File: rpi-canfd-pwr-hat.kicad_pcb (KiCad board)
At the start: 4 copper layers, 65 x 56 mm, 89 parts, among them J1 Conn_01x02, J2 Conn_01x04_Pin, J3 Raspberry_Pi, J4 Conn_01x02, J5 Conn_01x02, U1 XC6206P332MR, U10 SN74LV1T125DBV, U11 SN74LV1T125DBV, U12 SN74LV1T125DBV, U13 SN74LV1T125DBV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

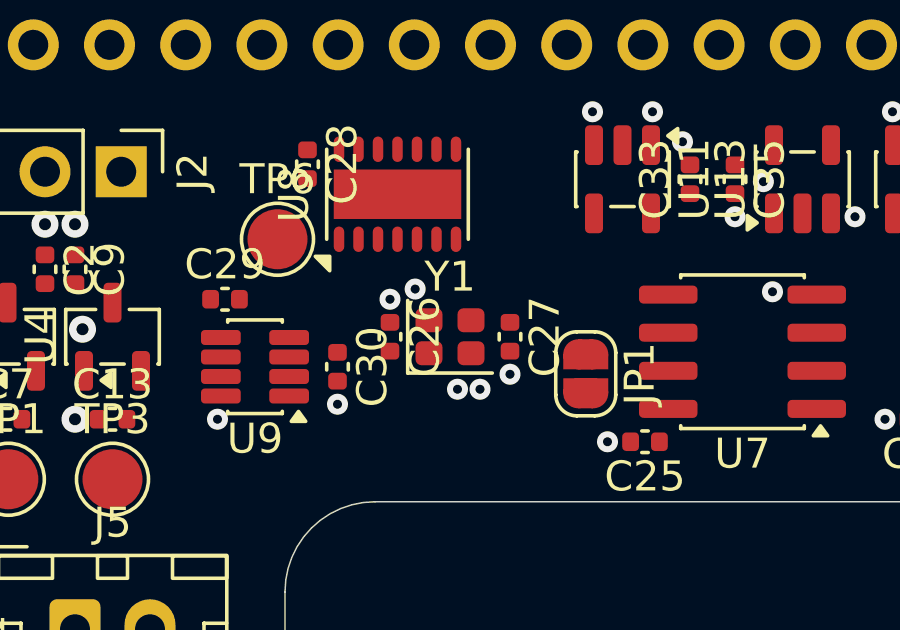
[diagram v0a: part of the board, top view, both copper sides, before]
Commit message: pcb: add xtal routing
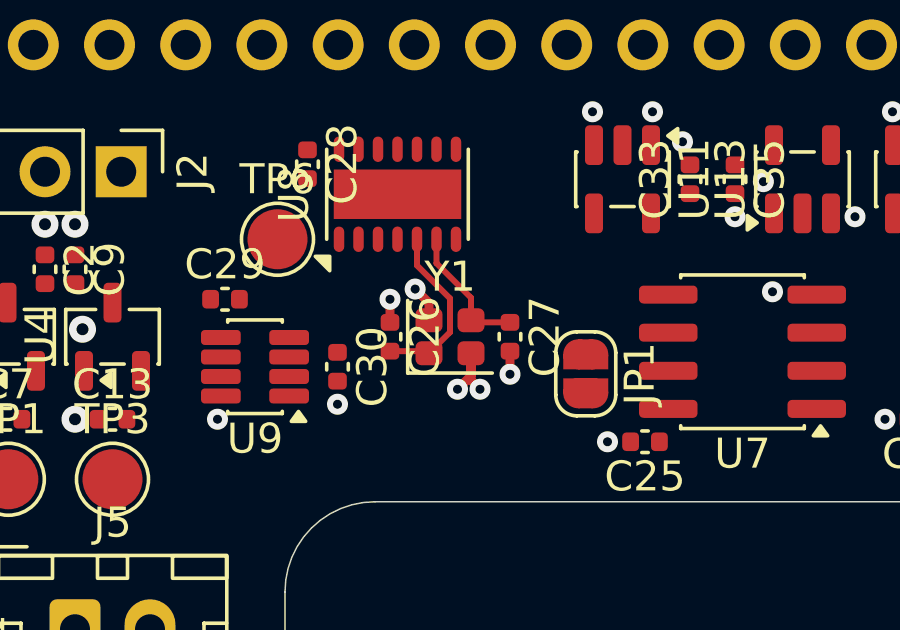
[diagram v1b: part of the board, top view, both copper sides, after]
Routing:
- net /XTAL_P: track 0.00 -> 5.87 mm
- net GND: track 0.00 -> 5.48 mm
- net /XTAL_N: track 0.00 -> 4.51 mm
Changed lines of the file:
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@@
 		(layer "Edge.Cuts")
+	)
+	(segment
+		(start 189.5 85.75)
+		(end 189.5 84.98)
+		(width 0.3)
+		(layer "F.Cu")
+		(net "GND")
+	)
+	(segment
+		(start 188.2 85.8)
+		(end 187.75 86.25)
+		(width 0.3)
+		(layer "F.Cu")
+		(net "GND")
+	)
+	(segment
+		(start 186.8 83.95)
+		(end 186.8 83.371099)
+		(width 0.3)
+		(layer "F.Cu")
+		(net "GND")
+	)
+	(segment
+		(start 185.5 84.02)
+		(end 185.5 83.25)
+		(width 0.3)
+		(layer "F.Cu")
+		(net "GND")
+	)
+	(segment
+		(start 188.2 85.05)
+		(end 188.2 85.95)
+		(width 0.3)
+		(layer "F.Cu")
+		(net "GND")
+	)
+	(segment
+		(start 188.2 85.95)
+		(end 188.5 86.25)
+		(width 0.3)
+		(layer "F.Cu")
+		(net "GND")
+	)
+	(segment
+		(start 186.8 83.371099)
+		(end 186.338833 82.909932)
+		(width 0.3)
+		(layer "F.Cu")
+		(net "GND")
+	)
+	(segment
+		(start 188.2 85.05)
+		(end 188.2 85.8)
+		(width 0.3)
+		(layer "F.Cu")
+		(net "GND")
 	)
 	(via
@@
 		(free yes)
 		(net "GND")
+	)
+	(segment
+		(start 187.5 84.35)
+		(end 186.8 85.05)
+		(width 0.2)
+		(layer "F.Cu")
+		(net "/XTAL_P")
+	)
+	(segment
+		(start 185.5 84.98)
+		(end 186.73 84.98)
+		(width 0.2)
+		(layer "F.Cu")
+		(net "/XTAL_P")
+	)
+	(segment
+		(start 186.4 82.12257)
+		(end 187.5 83.22257)
+		(width 0.2)
+		(layer "F.Cu")
+		(net "/XTAL_P")
+	)
+	(segment
+		(start 186.4 81.25)
+		(end 186.4 82.12257)
+		(width 0.2)
+		(layer "F.Cu")
+		(net "/XTAL_P")
+	)
+	(segment
+		(start 187.5 83.22257)
+		(end 187.5 84.35)
+		(width 0.2)
+		(layer "F.Cu")
+		(net "/XTAL_P")
+	)
+	(segment
+		(start 186.73 84.98)
+		(end 186.8 85.05)
+		(width 0.2)
+		(layer "F.Cu")
+		(net "/XTAL_P")
+	)
+	(segment
+		(start 188.2 83.2)
+		(end 187.05 82.05)
+		(width 0.2)
+		(layer "F.Cu")
+		(net "/XTAL_N")
+	)
+	(segment
+		(start 188.27 84.02)
+		(end 188.2 83.95)
+		(width 0.2)
+		(layer "F.Cu")
+		(net "/XTAL_N")
+	)
+	(segment
+		(start 189.5 84.02)
+		(end 188.27 84.02)
+		(width 0.2)
+		(layer "F.Cu")
+		(net "/XTAL_N")
+	)
+	(segment
+		(start 187.05 82.05)
+		(end 187.05 81.25)
+		(width 0.2)
+		(layer "F.Cu")
+		(net "/XTAL_N")
+	)
+	(segment
+		(start 188.2 83.95)
+		(end 188.2 83.2)
+		(width 0.2)
+		(layer "F.Cu")
+		(net "/XTAL_N")
 	)
 	(zone
@@
 			)
 		)
+	)
+	(zone
+		(layer "F.Cu")
+		(hatch edge 0.5)
+		(connect_pads
+			(clearance 0)
+		)
+		(min_thickness 0.25)
+		(keepout
+			(tracks allowed)
+			(vias allowed)
+			(pads allowed)
+			(copperpour not_allowed)
+			(footprints allowed)
+		)
+		(placement
+			(enabled no)
+			(sheetname "/")
+		)
+		(fill
+			(thermal_gap 0.5)
+			(thermal_bridge_width 0.5)
+			(island_removal_mode 0)
+		)
+		(polygon
+			(pts
+				(xy 189.25 82.5) (xy 190 83.25) (xy 190 86.25) (xy 189.5 86.75) (xy 186 86.75) (xy 185 85.75) (xy 185 83.25)
+				(xy 185.75 82.5)
+			)
+		)

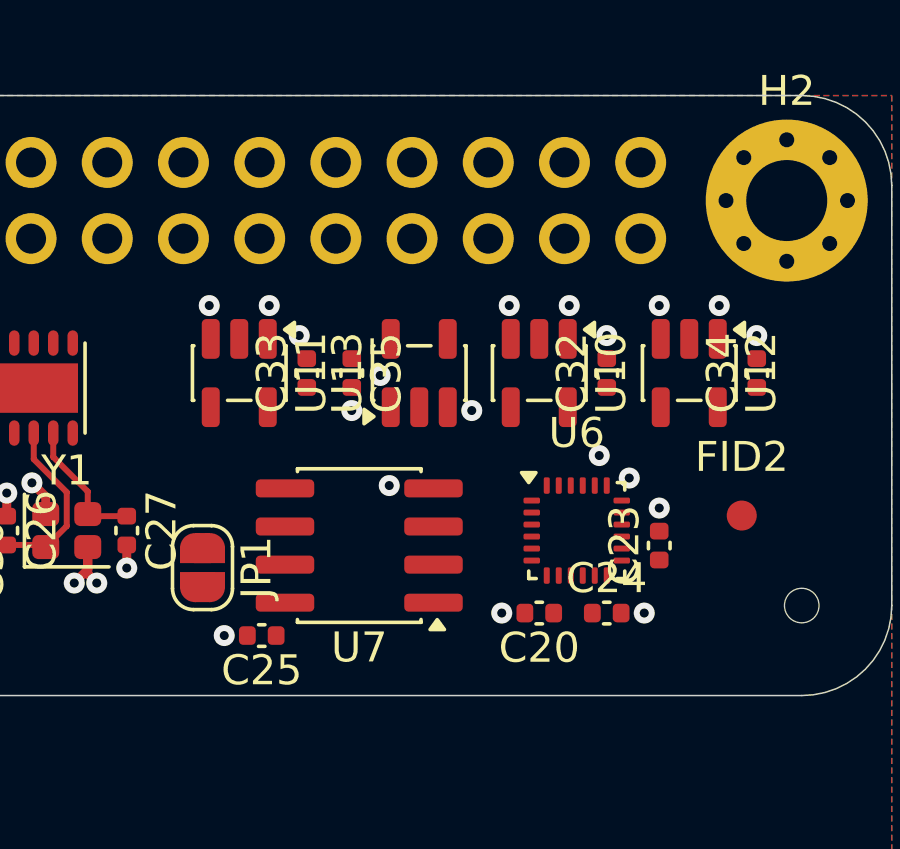
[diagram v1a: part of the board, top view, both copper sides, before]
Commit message: pcb: route imu
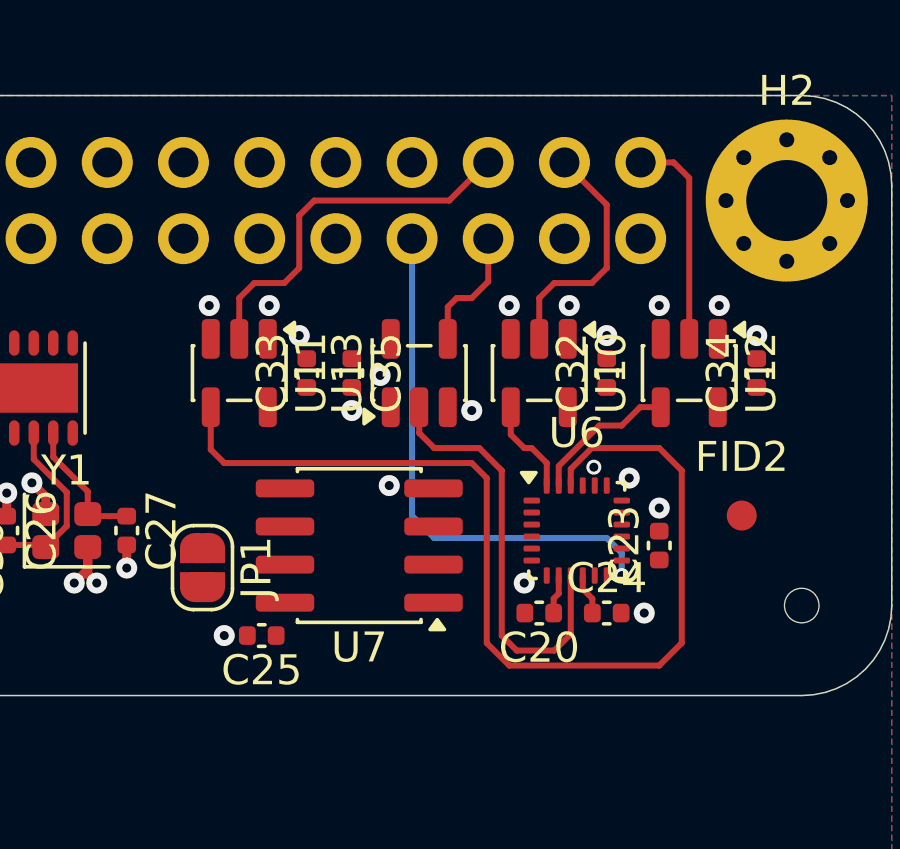
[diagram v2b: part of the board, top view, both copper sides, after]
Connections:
- J3 pad 12: /~{SPI2_CS} -> unconnected-(J3-GPIO18/SPI1_~{CE0}/PCM_CLK/PWM0-Pad12)
- J3 pad 22: /IMU_INT -> unconnected-(J3-GPIO25/SDIO_DAT1-Pad22)
- J3 pad 33: unconnected-(J3-GPIO13/PWM1-Pad33) -> /IMU_INT
- J3 pad 36: unconnected-(J3-GPIO16/SPI1_~{CE2}-Pad36) -> /~{SPI2_CS}
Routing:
- net /~{SPI2_CS}_1V8: track 0.00 -> 34.2 mm
- net /IMU_INT: track 0.00 -> 18.0 mm, vias 0 -> 1
- net /SPI2_MISO_1V8: track 0.00 -> 14.3 mm
- net /~{SPI2_CS}: track 0.00 -> 12.6 mm
- net /SPI2_MOSI: track 0.00 -> 8.13 mm
- net /SPI2_SCLK: track 0.00 -> 7.20 mm
- net /SPI2_SCLK_1V8: track 0.00 -> 4.86 mm
- net /SPI2_MISO: track 0.00 -> 4.19 mm
- net /SPI2_MOSI_1V8: track 0.00 -> 3.26 mm
- net Net-(U6-REGOUT): track 0.00 -> 1.38 mm
- net +1V8: track 0.00 -> 1.32 mm

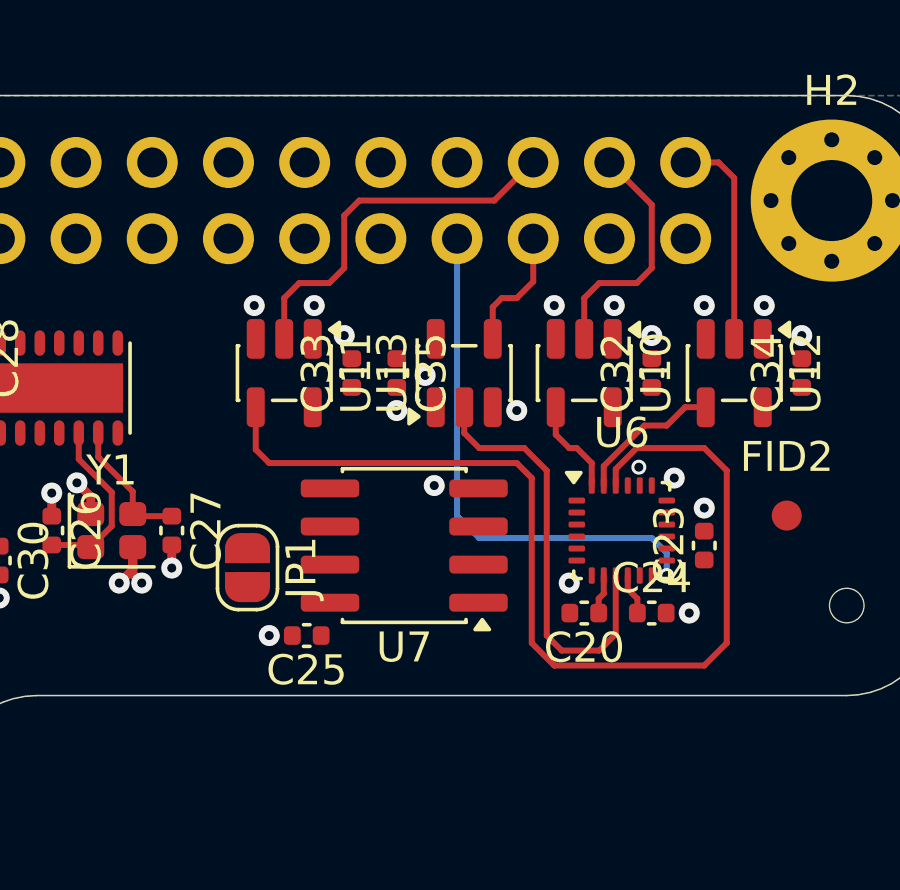
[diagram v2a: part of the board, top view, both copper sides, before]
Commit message: pcb: route eeprom
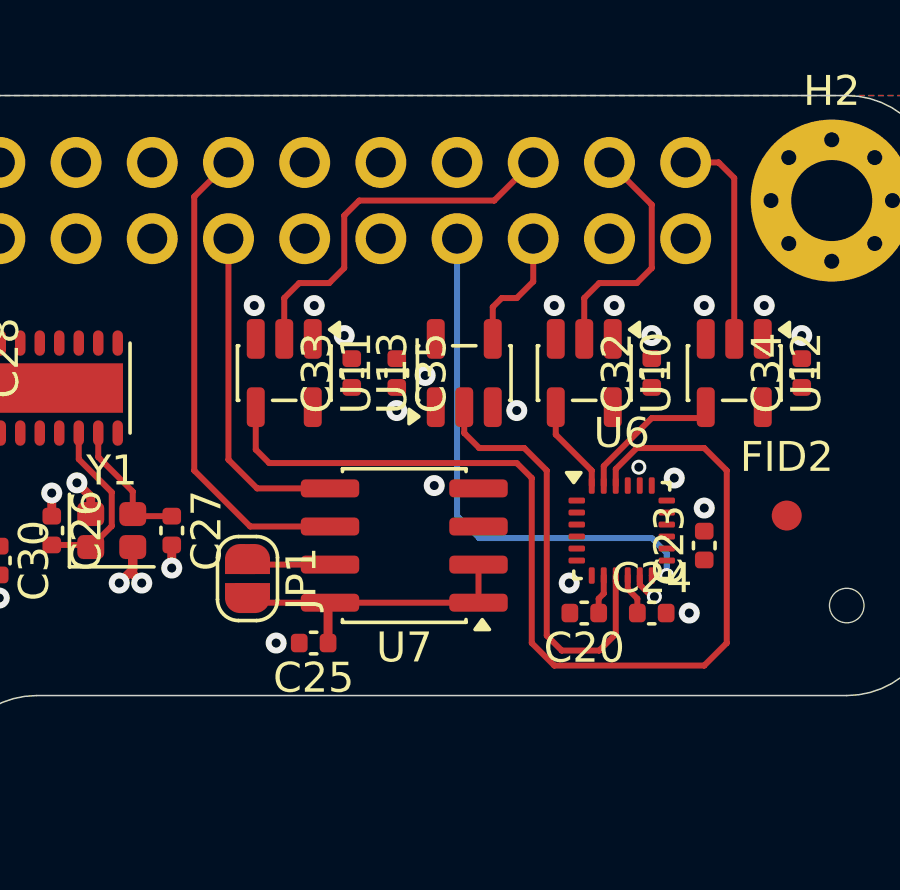
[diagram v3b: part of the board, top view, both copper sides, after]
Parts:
- moved JP1 0.36 mm to (192.0, 86.1)
- moved C25 0.34 mm to (194.2, 88.2)
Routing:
- net /SCL: track 0.00 -> 16.0 mm
- net /SDA: track 0.00 -> 11.2 mm
- net +3V3: track 0.00 -> 10.4 mm
- net Net-(JP1-A): track 0.00 -> 2.83 mm
- net GND: track 5.48 -> 6.44 mm, vias 75 -> 76
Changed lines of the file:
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@@
 	(footprint "Jumper:SolderJumper-2_P1.3mm_Open_RoundedPad1.0x1.5mm"
 		(layer "F.Cu")
-		(at 192.025 85.735 -90)
+		(at 192.025 86.1 -90)
 		(descr "SMD Solder Jumper, 1x1.5mm, rounded Pads, 0.3mm gap, open")
 		(tags "solder jumper open")
@@
 	(footprint "Capacitor_SMD:C_0402_1005Metric"
 		(layer "F.Cu")
-		(at 194 88 180)
+		(at 194.23 88.25 180)
 		(descr "Capacitor SMD 0402 (1005 Metric), square (rectangular) end terminal, IPC-7351 nominal, (Body size source: IPC-SM-782 page 76, https://www.pcb-3d.com/wordpress/wp-content/uploads/ipc-sm-782a_amendment_1_and_2.pdf)")
 		(tags "capacitor")
@@
 	)
 	(segment
+		(start 205.502917 86.703567)
+		(end 205.58807 86.703567)
+		(width 0.2)
+		(layer "F.Cu")
+		(net "GND")
+	)
+	(segment
 		(start 186.8 83.371099)
 		(end 186.338833 82.909932)
@@
 	)
 	(segment
+		(start 205.1 86)
+		(end 205.1 86.30065)
+		(width 0.2)
+		(layer "F.Cu")
+		(net "GND")
+	)
+	(segment
 		(start 188.2 85.05)
 		(end 188.2 85.8)
@@
 		(net "GND")
 	)
+	(segment
+		(start 205.1 86.30065)
+		(end 205.502917 86.703567)
+		(width 0.2)
+		(layer "F.Cu")
+		(net "GND")
+	)
 	(via
 		(at 171.75 84.25)
@@
 	)
 	(via
+		(at 205.58807 86.703567)
+		(size 0.5)
+		(drill 0.3)
+		(layers "F.Cu" "B.Cu")
+		(free yes)
+		(net "GND")
+	)
+	(via
 		(at 186.338833 82.909932)
 		(size 0.7)
@@
 	)
 	(via
-		(at 192.75 88)
+		(at 192.98 88.25)
 		(size 0.7)
 		(drill 0.3)
@@
 	)
 	(segment
+		(start 199.725 86.905)
+		(end 199.725 85.635)
+		(width 0.2)
+		(layer "F.Cu")
+		(net "+3V3")
+	)
+	(segment
+		(start 194.775 86.905)
+		(end 192.18 86.905)
+		(width 0.2)
+		(layer "F.Cu")
+		(net "+3V3")
+	)
+	(segment
+		(start 192.18 86.905)
+		(end 192.025 86.75)
+		(width 0.2)
+		(layer "F.Cu")
+		(net "+3V3")
+	)
+	(segment
+		(start 194.775 86.905)
+		(end 199.725 86.905)
+		(width 0.2)
+		(layer "F.Cu")
+		(net "+3V3")
+	)
+	(segment
+		(start 194.71 88.25)
+		(end 194.71 86.97)
+		(width 0.3)
+		(layer "F.Cu")
+		(net "+3V3")
+	)
+	(segment
+		(start 194.71 86.97)
+		(end 194.775 86.905)
+		(width 0.3)
+		(layer "F.Cu")
+		(net "+3V3")
+	)
+	(segment
 		(start 187.5 84.35)
 		(end 186.8 85.05)
@@
 	)
 	(segment
+		(start 194.775 85.635)
+		(end 192.21 85.635)
+		(width 0.2)
+		(layer "F.Cu")
+		(net "Net-(JP1-A)")
+	)
+	(segment
+		(start 192.21 85.635)
+		(end 192.025 85.45)
+		(width 0.2)
+		(layer "F.Cu")
+		(net "Net-(JP1-A)")
+	)
+	(segment
 		(start 207.73 72.23)
 		(end 206.63 72.23)
@@
 	)
 	(segment
-		(start 205.25 81)
+		(start 203.9 83)
 		(end 203.9 82.35)
 		(width 0.2)
@@
 	)
 	(segment
-		(start 206 81)
-		(end 205.25 81)
+		(start 207.25 80.75)
+		(end 207.25 80.4375)
 		(width 0.2)
 		(layer "F.Cu")
@@
 	)
 	(segment
-		(start 206.6125 80.3875)
-		(end 206 81)
+		(start 207.25 80.4375)
+		(end 207.3 80.3875)
 		(width 0.2)
 		(layer "F.Cu")
@@
 	)
 	(segment
-		(start 207.3 80.3875)
-		(end 206.6125 80.3875)
+		(start 203.9 82.35)
+		(end 205.5 80.75)
 		(width 0.2)
 		(layer "F.Cu")
@@
 	)
 	(segment
-		(start 203.9 82.35)
-		(end 203.9 83)
+		(start 205.5 80.75)
+		(end 207.25 80.75)
 		(width 0.2)
 		(layer "F.Cu")
@@
 	(segment
 		(start 203.5 83)
-		(end 203.5 82.25)
+		(end 203.5 82.5)
 		(width 0.2)
 		(layer "F.Cu")
@@
 	)
 	(segment
-		(start 202.75 81.75)
+		(start 203.5 82.5)
 		(end 202.3 81.3)
 		(width 0.2)
@@
 	)
 	(segment
-		(start 203.5 82.25)
-		(end 203 81.75)
+		(start 202.3 81.3)
+		(end 202.3 80.3875)
 		(width 0.2)
 		(layer "F.Cu")
@@
 	)
 	(segment
-		(start 203 81.75)
-		(end 202.75 81.75)
+		(start 194.775 83.095)
+		(end 192.345 83.095)
 		(width 0.2)
 		(layer "F.Cu")
-		(net "/SPI2_MOSI_1V8")
+		(net "/SDA")
 	)
 	(segment
-		(start 202.3 81.3)
-		(end 202.3 80.3875)
+		(start 191.39 82.14)
+		(end 191.39 74.77)
 		(width 0.2)
 		(layer "F.Cu")
-		(net "/SPI2_MOSI_1V8")
+		(net "/SDA")
+	)
+	(segment
+		(start 192.345 83.095)
+		(end 191.39 82.14)
+		(width 0.2)
+		(layer "F.Cu")
+		(net "/SDA")
+	)
+	(segment
+		(start 192.115 84.365)
+		(end 190.25 82.5)
+		(width 0.2)
+		(layer "F.Cu")
+		(net "/SCL")
+	)
+	(segment
+		(start 194.775 84.365)
+		(end 192.115 84.365)
+		(width 0.2)
+		(layer "F.Cu")
+		(net "/SCL")
+	)
+	(segment
+		(start 190.25 73.37)
+		(end 191.39 72.23)
+		(width 0.2)
+		(layer "F.Cu")
+		(net "/SCL")
+	)
+	(segment
+		(start 190.25 82.5)
+		(end 190.25 73.37)
+		(width 0.2)
+		(layer "F.Cu")
+		(net "/SCL")
 	)
 	(segment
